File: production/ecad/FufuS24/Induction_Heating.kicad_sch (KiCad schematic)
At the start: 18 parts, among them IC1 FOD3150, J1 Conn_01x02, U3 STGP8NC60KD, U8 AD8561

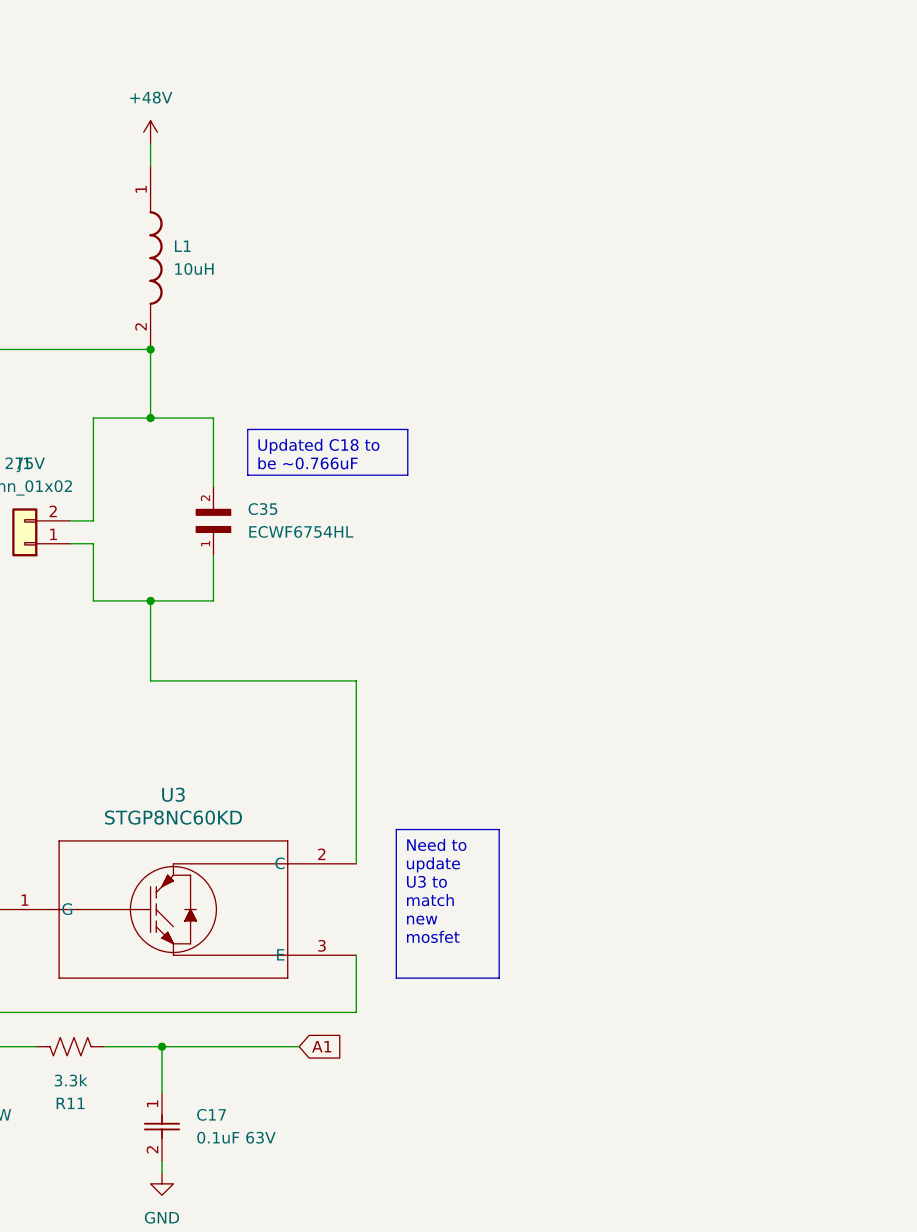
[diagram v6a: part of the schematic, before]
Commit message: Design review changes
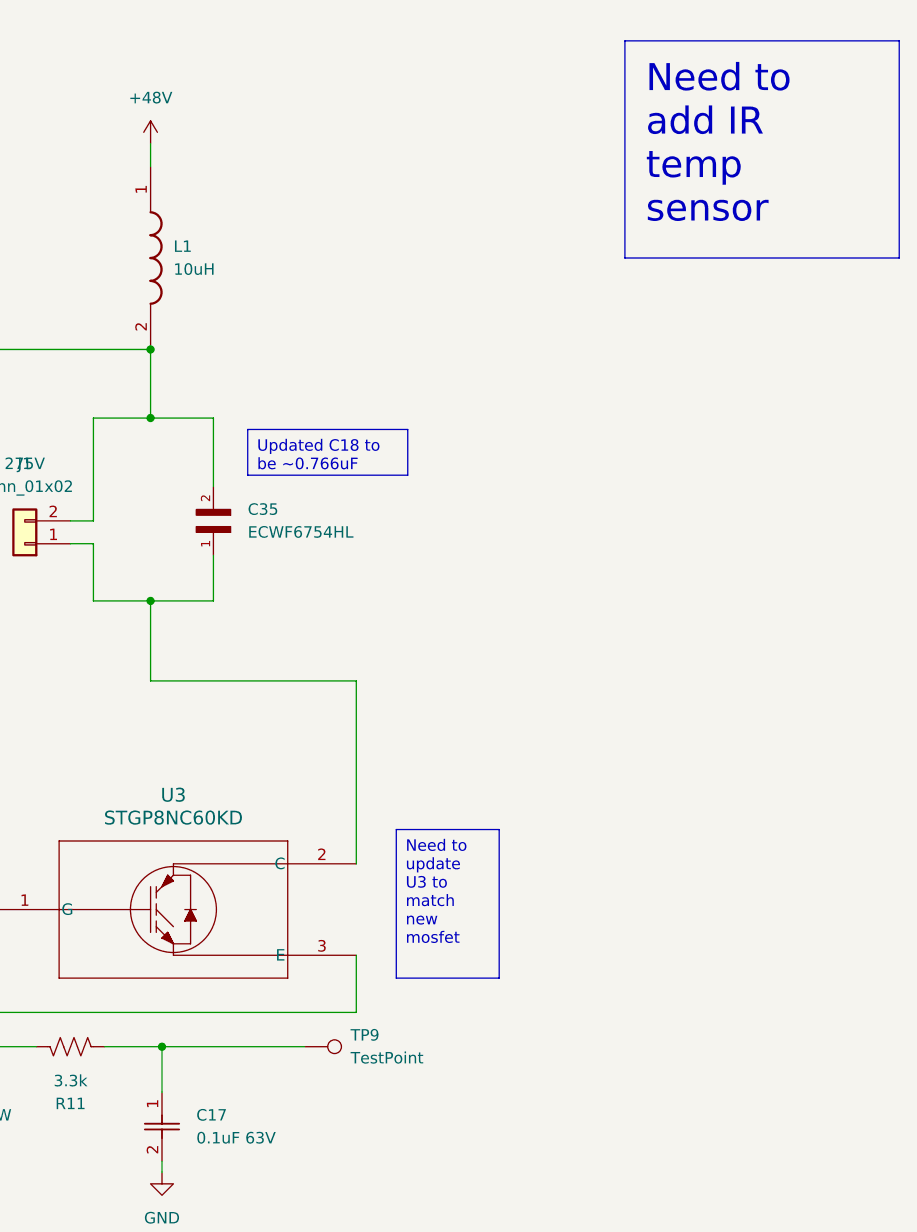
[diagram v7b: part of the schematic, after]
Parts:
- added TP9: TestPoint, TestPoint:TestPoint_Pad_2.0x2.0mm, symbol Connector:TestPoint
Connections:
- net A1: no longer names the net of C17.1, R11.2
- net A1: now also TP9.1
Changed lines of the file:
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@@
     (stroke (width 0) (type default))
   )
-  (wire (pts (xy 189.865 130.81) (xy 205.105 130.81))
+  (wire (pts (xy 189.865 130.81) (xy 205.74 130.81))
     (stroke (width 0) (type default))
   )
@@
     (fill (type none))
     (effects (font (size 1.27 1.27)) (justify left top))
+  )
+  (text_box "Need to add IR temp sensor\n"
+    (at 241.3 19.05 0) (size 30.48 24.13)
+    (stroke (width 0) (type default))
+    (fill (type none))
+    (effects (font (size 3 3)) (justify left top))
   )
   (text_box "The TLV7041-Q1 has a super low (nA) supply current so that could be a good option instead of this\n"
@@
     )
   )
-  (global_label "A1" (shape input) (at 205.105 130.81 0) (fields_autoplaced)
-    (effects (font (size 1.27 1.27)) (justify left))
-    (property "Intersheetrefs" "${INTERSHEET_REFS}" (at 210.3883 130.81 0)
-      (effects (font (size 1.27 1.27)) (justify left) hide)
-    )
-  )
   (symbol (lib_id "power:GND") (at 189.865 144.78 0) (unit 1)
     (in_bom yes) (on_board yes) (dnp no) (fields_autoplaced)
@@
         )
       )
+    )
+  )
+  (symbol (lib_id "Connector:TestPoint") (at 205.74 130.81 270) (unit 1)
+    (in_bom yes) (on_board yes) (dnp no) (fields_autoplaced)
+    (property "Reference" "TP9" (at 210.82 129.54 90)
+      (effects (font (size 1.27 1.27)) (justify left))
+    )
+    (property "Value" "TestPoint" (at 210.82 132.08 90)
+      (effects (font (size 1.27 1.27)) (justify left))
+    )
+    (property "Footprint" "TestPoint:TestPoint_Pad_2.0x2.0mm" (at 205.74 135.89 0)
+      (effects (font (size 1.27 1.27)) hide)
+    )
+    (property "Datasheet" "~" (at 205.74 135.89 0)
+      (effects (font (size 1.27 1.27)) hide)
+    )
+    (pin "1")
+    (instances
+      (project "FufuS24"
+        (path "/c4c3980b-c8c0-435e-abdc-bbed2349d7ac/57fb5dcd-e779-40d3-8741-57c7eee1ca58"
+          (reference "TP9") (unit 1)
+        )
+      )

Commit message: Ethan Stuff
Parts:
- added C18: 0.1uF 63V, 8600footprint:CAP_WCAP-ATG5_05.0X11.0_WRE, symbol 2023-11-09_20-51-41:860020772001
- added M1: MLX90614ESF-AAA-000-TU, MLX90614ESF-AAA-000-TU:TO254P942H425-4, symbol MLX90614ESF-AAA-000-TU:MLX90614ESF-AAA-000-TU
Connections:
- net +5V: now also C18.1, M1.3 (VDD)
- net GND: now also C18.2, M1.4 (VSS)
- new net INFRARED_SCL: M1.1 (SCL/VZ)
- new net INFRARED_SDA: M1.2 (SDA/PWM)
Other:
- note added: "Heat Warning LED"
- note added: "Induction Circuit"
- note added: "Temperature Sensing"
- moved on the sheet: C17, C34, C35, C4, D1, D2, IC1, J1, L1, R11, R19, R6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
